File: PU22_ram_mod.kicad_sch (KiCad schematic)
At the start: 7 parts, among them J1 MOBO, J2 BA8, J3 BA10

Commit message: Update schematic
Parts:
- added C1, C2, C3, C4: 100nF, Capacitor_SMD:C_1206_3216Metric_Pad1.33x1.80mm_HandSolder, symbol Device:C_Small
- J2, J3: footprint TestPoint:TestPoint_Pad_D4.0mm -> TestPoint:TestPoint_Pad_D2.5mm
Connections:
- net A0: now also U1.10 (A0), U2.10 (A0), U3.10 (A0), U4.10 (A0)
- net A1: now also U1.11 (A1), U2.11 (A1), U3.11 (A1), U4.11 (A1)
- net A10: now also U1.9 (A10), U2.9 (A10), U3.9 (A10), U4.9 (A10)
- net A2: now also U1.12 (A2), U2.12 (A2), U3.12 (A2), U4.12 (A2)
- net A3: now also U1.13 (A3), U2.13 (A3), U3.13 (A3), U4.13 (A3)
- net A4: now also U1.16 (A4), U2.16 (A4), U3.16 (A4), U4.16 (A4)
- net A5: now also U1.17 (A5), U2.17 (A5), U3.17 (A5), U4.17 (A5)
- net A6: now also U1.18 (A6), U2.18 (A6), U3.18 (A6), U4.18 (A6)
- net A7: now also U1.19 (A7), U2.19 (A7), U3.19 (A7), U4.19 (A7)
- net A8: now also U1.20 (A8), U2.20 (A8), U3.20 (A8), U4.20 (A8)
- net A9: now also U1.21 (A9), U2.21 (A9), U3.21 (A9), U4.21 (A9)
- net D0: now also U1.2 (DQ1)
- net D1: now also U1.3 (DQ2)
- net D10: now also U2.4 (DQ3)
- net D11: now also U2.5 (DQ4)
- net D12: now also U2.24 (DQ5)
- net D13: now also U2.25 (DQ6)
- net D14: now also U2.26 (DQ7)
- net D15: now also U2.27 (DQ8)
- net D17: now also U3.2 (DQ1)
- net D18: now also U3.3 (DQ2)
- net D19: now also U3.4 (DQ3)
- net D2: now also U1.4 (DQ3)
- net D20: now also U3.5 (DQ4)
- net D21: now also U3.24 (DQ5)
- net D22: now also U3.25 (DQ6)
- net D23: now also U3.26 (DQ7)
- net D24: now also U3.27 (DQ8)
- net D25: now also U4.2 (DQ1)
- net D26: now also U4.3 (DQ2)
- net D27: now also U4.4 (DQ3)
- net D28: now also U4.5 (DQ4)
- net D29: now also U4.24 (DQ5)
- net D3: now also U1.5 (DQ4)
- net D30: now also U4.25 (DQ6)
- net D31: now also U4.26 (DQ7)
- net D4: now also U1.24 (DQ5)
- net D5: now also U1.25 (DQ6)
- net D6: now also U1.26 (DQ7)
- net D7: now also U1.27 (DQ8)
- net D8: now also U2.2 (DQ1)
- net D9: now also U2.3 (DQ2)
- net GND: now also U1.15 (Vss), U1.28 (Vss), U2.15 (Vss), U2.28 (Vss), U3.15 (Vss), U3.28 (Vss), U4.15 (Vss), U4.28 (Vss), C1.2, C2.2, C3.2, C4.2
- net VCC: now also U1.1 (Vdd), U1.14 (Vdd), U2.1 (Vdd), U2.14 (Vdd), U3.1 (Vdd), U3.14 (Vdd), U4.1 (Vdd), U4.14 (Vdd), C1.1, C2.1, C3.1, C4.1
- net ~{CAS1}: now also U1.23 (~{CAS})
- net ~{CAS2}: now also U2.23 (~{CAS})
- net ~{CAS3}: now also U3.23 (~{CAS})
- net ~{CAS4}: now also U4.23 (~{CAS})
- net ~{OE}: now also U1.22 (~{OE}), U2.22 (~{OE}), U3.22 (~{OE}), U4.22 (~{OE})
- net ~{RAS}: now also U1.7 (~{RAS}), U2.7 (~{RAS}), U3.7 (~{RAS}), U4.7 (~{RAS})
- net ~{WE}: now also U1.6 (~{W}), U2.6 (~{W}), U3.6 (~{W}), U4.6 (~{W})
- net D32: now reaches U4.27 (DQ8)
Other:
- moved on the sheet: J1, J2, J3, U1, U2, U3, U4

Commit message: Some routing
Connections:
- net D32 is gone; now on net D31: U4.27 (DQ8)
- net D16: now also U3.2 (DQ1)
- net D17: now also U3.3 (DQ2); no longer U3.2 (DQ1)
- net D18: now also U3.4 (DQ3); no longer U3.3 (DQ2)
- net D19: now also U3.5 (DQ4); no longer U3.4 (DQ3)
- net D20: now also U3.24 (DQ5); no longer U3.5 (DQ4)
- net D21: now also U3.25 (DQ6); no longer U3.24 (DQ5)
- net D22: now also U3.26 (DQ7); no longer U3.25 (DQ6)
- net D23: now also U3.27 (DQ8); no longer U3.26 (DQ7)
- net D24: now also U4.2 (DQ1); no longer U3.27 (DQ8)
- net D25: now also U4.3 (DQ2); no longer U4.2 (DQ1)
- net D26: now also U4.4 (DQ3); no longer U4.3 (DQ2)
- net D27: now also U4.5 (DQ4); no longer U4.4 (DQ3)
- net D28: now also U4.24 (DQ5); no longer U4.5 (DQ4)
- net D29: now also U4.25 (DQ6); no longer U4.24 (DQ5)
- net D30: now also U4.26 (DQ7); no longer U4.25 (DQ6)
- net D31: no longer U4.26 (DQ7)
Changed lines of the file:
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@@
 	(wire
 		(pts
-			(xy 80.01 140.97) (xy 90.17 140.97)
+			(xy 80.01 143.51) (xy 90.17 143.51)
 		)
 		(stroke
@@
 	(wire
 		(pts
-			(xy 128.27 140.97) (xy 138.43 140.97)
+			(xy 128.27 143.51) (xy 138.43 143.51)
 		)
 		(stroke
@@
 	(wire
 		(pts
+			(xy 80.01 125.73) (xy 90.17 125.73)
+		)
+		(stroke
+			(width 0)
+			(type default)
+		)
+	)
+	(wire
+		(pts
 			(xy 96.52 143.51) (xy 105.41 143.51)
 		)
@@
 	(wire
 		(pts
-			(xy 80.01 128.27) (xy 90.17 128.27)
+			(xy 80.01 130.81) (xy 90.17 130.81)
 		)
 		(stroke
@@
 	(wire
 		(pts
-			(xy 80.01 130.81) (xy 90.17 130.81)
+			(xy 80.01 133.35) (xy 90.17 133.35)
 		)
 		(stroke
@@
 	(wire
 		(pts
-			(xy 80.01 143.51) (xy 90.17 143.51)
+			(xy 128.27 125.73) (xy 138.43 125.73)
 		)
 		(stroke
@@
 	(wire
 		(pts
-			(xy 128.27 135.89) (xy 138.43 135.89)
+			(xy 128.27 138.43) (xy 138.43 138.43)
 		)
 		(stroke
@@
 	(wire
 		(pts
-			(xy 80.01 133.35) (xy 90.17 133.35)
+			(xy 80.01 135.89) (xy 90.17 135.89)
 		)
 		(stroke
@@
 	(wire
 		(pts
-			(xy 128.27 143.51) (xy 138.43 143.51)
-		)
-		(stroke
-			(width 0)
-			(type default)
-		)
-	)
-	(wire
-		(pts
 			(xy 219.71 59.69) (xy 228.6 59.69)
 		)
@@
 	(wire
 		(pts
-			(xy 128.27 138.43) (xy 138.43 138.43)
+			(xy 128.27 140.97) (xy 138.43 140.97)
 		)
 		(stroke
@@
 	(wire
 		(pts
-			(xy 128.27 133.35) (xy 138.43 133.35)
+			(xy 128.27 135.89) (xy 138.43 135.89)
 		)
 		(stroke
@@
 	(wire
 		(pts
-			(xy 80.01 138.43) (xy 90.17 138.43)
+			(xy 80.01 140.97) (xy 90.17 140.97)
 		)
 		(stroke
@@
 	(wire
 		(pts
-			(xy 128.27 130.81) (xy 138.43 130.81)
+			(xy 128.27 133.35) (xy 138.43 133.35)
 		)
 		(stroke
@@
 	(wire
 		(pts
-			(xy 128.27 125.73) (xy 138.43 125.73)
+			(xy 128.27 128.27) (xy 138.43 128.27)
 		)
 		(stroke
@@
 	(wire
 		(pts
-			(xy 80.01 135.89) (xy 90.17 135.89)
+			(xy 80.01 138.43) (xy 90.17 138.43)
 		)
 		(stroke
@@
 	(wire
 		(pts
-			(xy 128.27 128.27) (xy 138.43 128.27)
+			(xy 128.27 130.81) (xy 138.43 130.81)
 		)
 		(stroke
@@
 	(wire
 		(pts
-			(xy 80.01 125.73) (xy 90.17 125.73)
+			(xy 80.01 128.27) (xy 90.17 128.27)
 		)
 		(stroke
@@
 	)
 	(label "D21"
-		(at 90.17 135.89 180)
+		(at 90.17 138.43 180)
 		(fields_autoplaced yes)
 		(effects
@@
 		)
 	)
-	(label "D32"
-		(at 138.43 143.51 180)
-		(fields_autoplaced yes)
-		(effects
-			(font
-				(size 1.27 1.27)
-			)
-			(justify right bottom)
-		)
-	)
 	(label "D27"
 		(at 228.6 57.15 180)
@@
 	)
 	(label "D30"
-		(at 138.43 138.43 180)
+		(at 138.43 140.97 180)
 		(fields_autoplaced yes)
 		(effects
@@
 	)
 	(label "D17"
-		(at 90.17 125.73 180)
+		(at 90.17 128.27 180)
 		(fields_autoplaced yes)
 		(effects
@@
 	)
 	(label "D20"
-		(at 90.17 133.35 180)
+		(at 90.17 135.89 180)
 		(fields_autoplaced yes)
 		(effects
@@
 	)
 	(label "D22"
-		(at 90.17 138.43 180)
+		(at 90.17 140.97 180)
 		(fields_autoplaced yes)
 		(effects
@@
 	)
 	(label "D26"
-		(at 138.43 128.27 180)
+		(at 138.43 130.81 180)
 		(fields_autoplaced yes)
 		(effects
@@
 	)
 	(label "D24"
-		(at 90.17 143.51 180)
+		(at 138.43 125.73 180)
 		(fields_autoplaced yes)
 		(effects
@@
 		)
 	)
+	(label "D16"
+		(at 90.17 125.73 180)
+		(fields_autoplaced yes)
+		(effects
+			(font
+				(size 1.27 1.27)
+			)
+			(justify right bottom)
+		)
+	)
 	(label "D18"
-		(at 90.17 128.27 180)
+		(at 90.17 130.81 180)
 		(fields_autoplaced yes)
 		(effects
@@
 	)
 	(label "D25"
-		(at 138.43 125.73 180)
+		(at 138.43 128.27 180)
 		(fields_autoplaced yes)
 		(effects
@@
 	)
 	(label "D19"
-		(at 90.17 130.81 180)
+		(at 90.17 133.35 180)
 		(fields_autoplaced yes)
 		(effects
@@
 	)
 	(label "D31"
-		(at 138.43 140.97 180)
+		(at 138.43 143.51 180)
 		(fields_autoplaced yes)
 		(effects
@@
 	)
 	(label "D29"
-		(at 138.43 135.89 180)
+		(at 138.43 138.43 180)
 		(fields_autoplaced yes)
 		(effects
@@
 	)
 	(label "D27"
-		(at 138.43 130.81 180)
+		(at 138.43 133.35 180)
 		(fields_autoplaced yes)
 		(effects
@@
 	)
 	(label "D23"
-		(at 90.17 140.97 180)
+		(at 90.17 143.51 180)
 		(fields_autoplaced yes)
 		(effects
@@
 	)
 	(label "D28"
-		(at 138.43 133.35 180)
+		(at 138.43 135.89 180)
 		(fields_autoplaced yes)
 		(effects

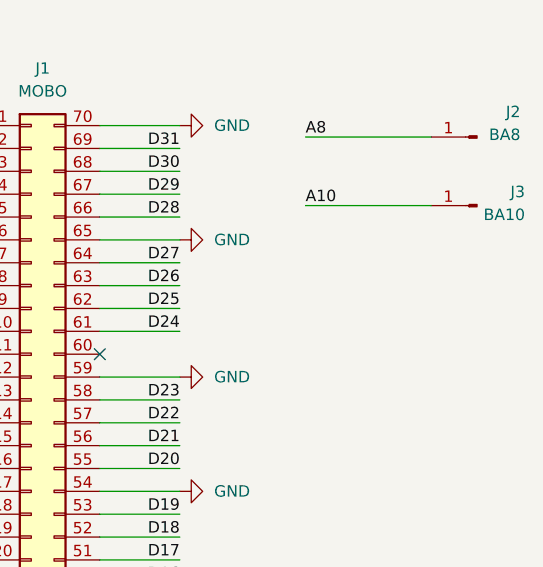
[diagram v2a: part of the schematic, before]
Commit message: Add copper fill in the zone with RAMs
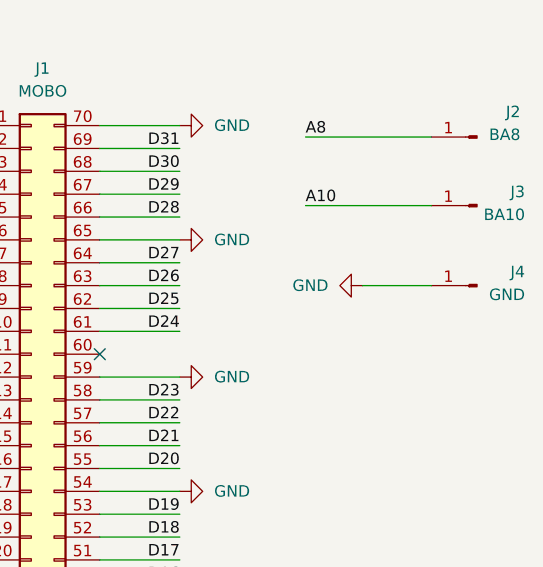
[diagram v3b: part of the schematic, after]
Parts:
- added J4: GND, TestPoint:TestPoint_Pad_D2.5mm, symbol Connector:Conn_01x01_Pin
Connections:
- net GND: now also J4.1 (Pin_1)
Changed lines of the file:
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@@
 	(wire
 		(pts
+			(xy 248.92 59.69) (xy 256.54 59.69)
+		)
+		(stroke
+			(width 0)
+			(type default)
+		)
+	)
+	(wire
+		(pts
 			(xy 68.58 95.25) (xy 68.58 93.98)
 		)
@@
 	)
 	(symbol
+		(lib_id "Connector:Conn_01x01_Pin")
+		(at 261.62 59.69 180)
+		(unit 1)
+		(exclude_from_sim no)
+		(in_bom yes)
+		(on_board yes)
+		(dnp no)
+		(property "Reference" "J4"
+			(at 266.954 58.166 0)
+			(effects
+				(font
+					(size 1.27 1.27)
+				)
+				(justify left)
+			)
+		)
+		(property "Value" "GND"
+			(at 266.954 60.706 0)
+			(effects
+				(font
+					(size 1.27 1.27)
+				)
+				(justify left)
+			)
+		)
+		(property "Footprint" "TestPoint:TestPoint_Pad_D2.5mm"
+			(at 261.62 59.69 0)
+			(effects
+				(font
+					(size 1.27 1.27)
+				)
+				(hide yes)
+			)
+		)
+		(property "Datasheet" "~"
+			(at 261.62 59.69 0)
+			(effects
+				(font
+					(size 1.27 1.27)
+				)
+				(hide yes)
+			)
+		)
+		(property "Description" "Generic connector, single row, 01x01, script generated"
+			(at 261.62 59.69 0)
+			(effects
+				(font
+					(size 1.27 1.27)
+				)
+				(hide yes)
+			)
+		)
+		(pin "1"
+		)
+		(instances
+			(project "PU22_ram_mod"
+				(path "/511ef809-acff-4cc5-af0e-950e48ca57ea"
+					(reference "J4")
+					(unit 1)
+				)
+			)
+		)
+	)
+	(symbol
 		(lib_id "Device:C_Small")
 		(at 190.5 147.32 0)
@@
 					(unit 1)
 				)
+			)
+		)
+	)
+	(symbol
+		(lib_id "power:GND")
+		(at 248.92 59.69 270)
+		(unit 1)
+		(exclude_from_sim no)
+		(in_bom yes)
+		(on_board yes)
+		(dnp no)
+		(fields_autoplaced yes)
+		(property "Reference" "#PWR021"
+			(at 242.57 59.69 0)
+			(effects
+				(font
+					(size 1.27 1.27)
+				)
+				(hide yes)
+			)
+		)
+		(property "Value" "GND"
+			(at 245.11 59.6899 90)
+			(effects
+				(font
+					(size 1.27 1.27)
+				)
+				(justify right)
+			)
+		)
+		(property "Footprint" ""
+			(at 248.92 59.69 0)
+			(effects
+				(font
+					(size 1.27 1.27)
+				)
+				(hide yes)
+			)
+		)
+		(property "Datasheet" ""
+			(at 248.92 59.69 0)
+			(effects
+				(font
+					(size 1.27 1.27)
+				)
+				(hide yes)
+			)
+		)
+		(property "Description" "Power symbol creates a global label with name \"GND\" , ground"
+			(at 248.92 59.69 0)
+			(effects
+				(font
+					(size 1.27 1.27)
+				)
+				(hide yes)
+			)
+		)
+		(pin "1"
+		)
+		(instances
+			(project ""
+				(path "/511ef809-acff-4cc5-af0e-950e48ca57ea"
+					(reference "#PWR021")
+					(unit 1)
+				)
